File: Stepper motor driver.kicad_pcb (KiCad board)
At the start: 2 copper layers, 63 x 74.4 mm, 24 parts, among them Q1 TIP120, Q2 TIP120, Q3 TIP120, Q4 TIP120, U1 74LS175, U2 74LS157

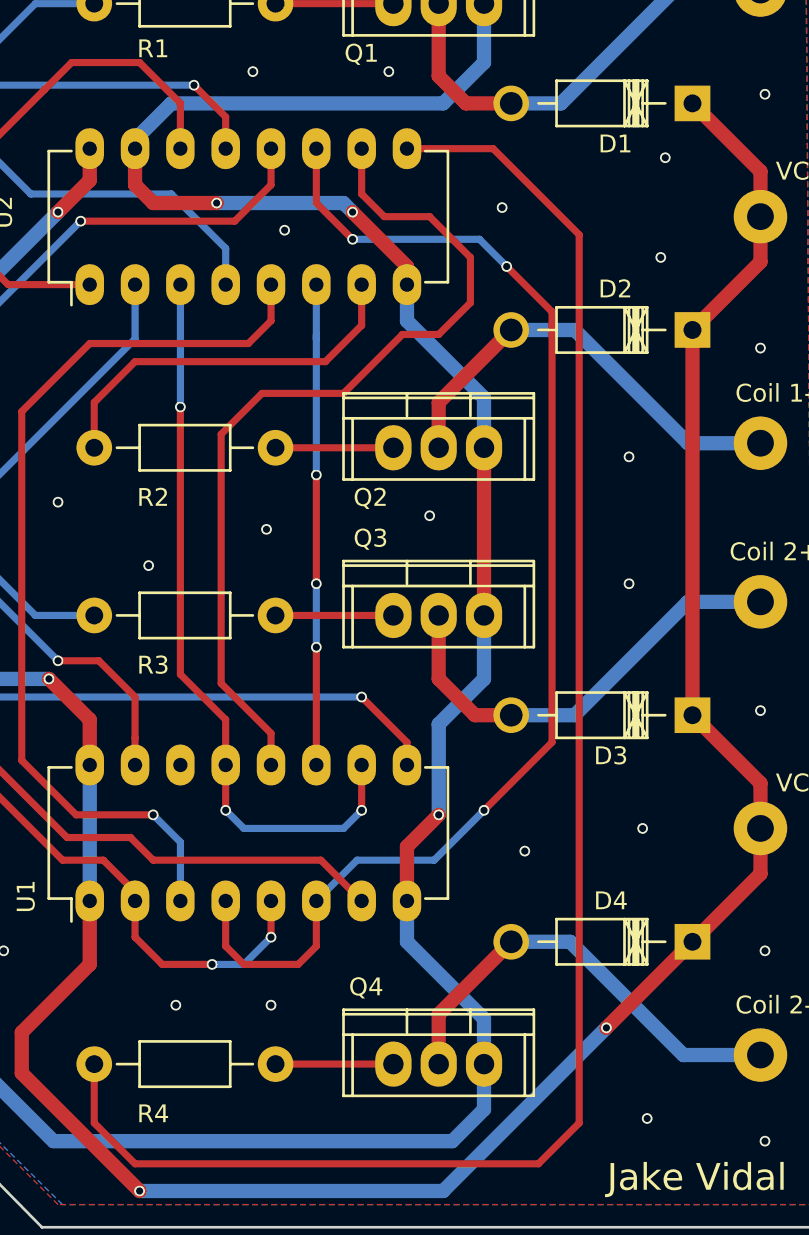
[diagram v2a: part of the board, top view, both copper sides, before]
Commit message: added additional vias
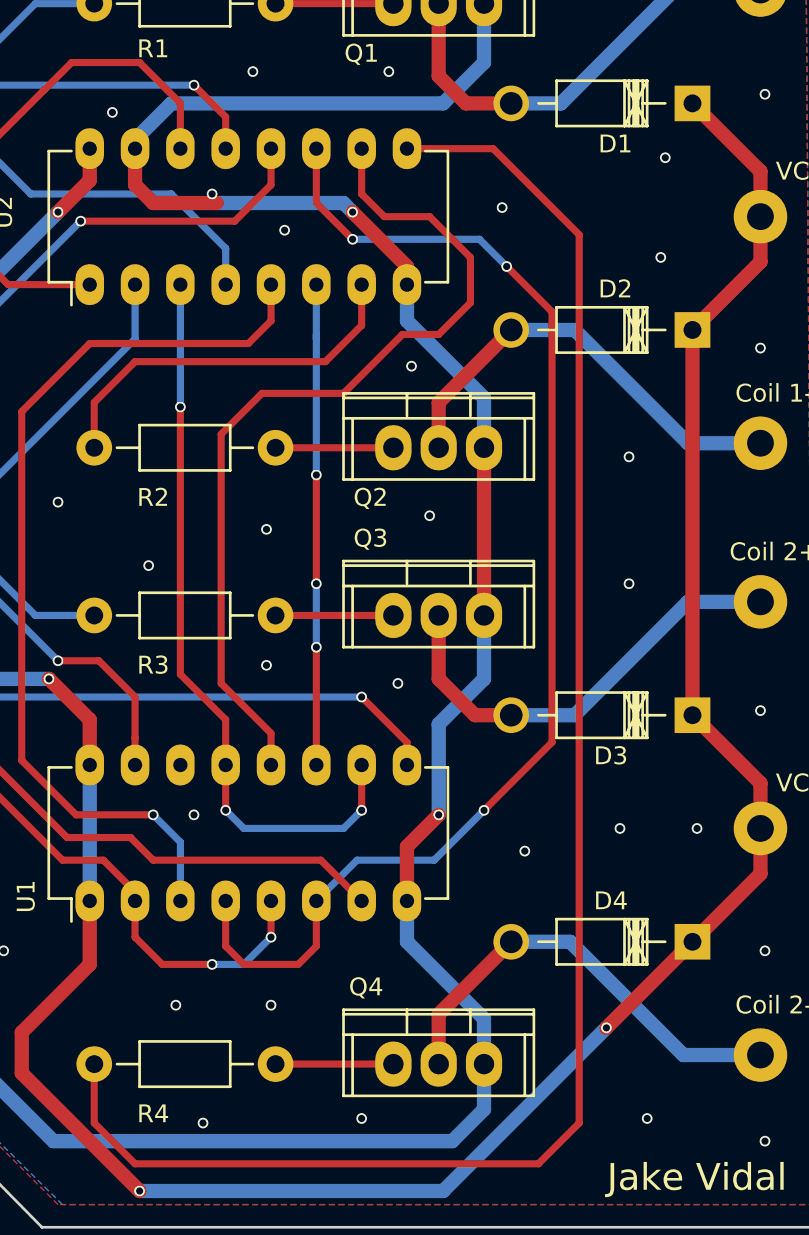
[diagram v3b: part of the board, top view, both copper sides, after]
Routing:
- net GND: vias 39 -> 4
- net (no net): vias 0 -> 43
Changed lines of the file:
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@@
     (thickness 1.6)
     (drawings 7)
-    (tracks 290)
+    (tracks 298)
     (zones 0)
     (modules 24)
@@
   (gr_line (start 215 20.32) (end 196.596 38) (angle 90) (layer Edge.Cuts) (width 0.15))
   (gr_line (start 259.588 20.32) (end 215 20.32) (angle 90) (layer Edge.Cuts) (width 0.15))
+  (via (at 235.712 46.482) (size 0.6) (drill 0.4) (layers F.Cu B.Cu) (net 0))
+  (via (at 251.714 72.39) (size 0.6) (drill 0.4) (layers F.Cu B.Cu) (net 0))
+  (via (at 228.6 38.862) (size 0.6) (drill 0.4) (layers F.Cu B.Cu) (net 0))
+  (via (at 240.792 37.592) (size 0.6) (drill 0.4) (layers F.Cu B.Cu) (net 0))
+  (via (at 255.524 89.916) (size 0.6) (drill 0.4) (layers F.Cu B.Cu) (net 0))
+  (via (at 207.01 72.39) (size 0.6) (drill 0.4) (layers F.Cu B.Cu) (net 0))
+  (via (at 212.09 73.66) (size 0.6) (drill 0.4) (layers F.Cu B.Cu) (net 0))
+  (via (at 207.772 63.246) (size 0.6) (drill 0.4) (layers F.Cu B.Cu) (net 0))
+  (via (at 200.914 68.326) (size 0.6) (drill 0.4) (layers F.Cu B.Cu) (net 0))
+  (via (at 200.406 56.896) (size 0.6) (drill 0.4) (layers F.Cu B.Cu) (net 0))
+  (via (at 206.248 54.356) (size 0.6) (drill 0.4) (layers F.Cu B.Cu) (net 0))
+  (via (at 206.756 41.402) (size 0.6) (drill 0.4) (layers F.Cu B.Cu) (net 0))
+  (via (at 199.39 44.958) (size 0.6) (drill 0.4) (layers F.Cu B.Cu) (net 0))
+  (via (at 205.486 35.052) (size 0.6) (drill 0.4) (layers F.Cu B.Cu) (net 0))
+  (via (at 216.408 23.622) (size 0.6) (drill 0.4) (layers F.Cu B.Cu) (net 0))
+  (via (at 226.314 23.368) (size 0.6) (drill 0.4) (layers F.Cu B.Cu) (net 0))
+  (via (at 226.822 29.972) (size 0.6) (drill 0.4) (layers F.Cu B.Cu) (net 0))
+  (via (at 234.442 29.972) (size 0.6) (drill 0.4) (layers F.Cu B.Cu) (net 0))
+  (via (at 245.872 24.384) (size 0.6) (drill 0.4) (layers F.Cu B.Cu) (net 0))
+  (via (at 255.524 31.242) (size 0.6) (drill 0.4) (layers F.Cu B.Cu) (net 0))
+  (via (at 249.936 34.798) (size 0.6) (drill 0.4) (layers F.Cu B.Cu) (net 0))
+  (via (at 249.682 40.386) (size 0.6) (drill 0.4) (layers F.Cu B.Cu) (net 0))
+  (via (at 255.27 45.466) (size 0.6) (drill 0.4) (layers F.Cu B.Cu) (net 0))
+  (via (at 215.9 54.102) (size 0.6) (drill 0.4) (layers F.Cu B.Cu) (net 0))
+  (via (at 220.98 57.658) (size 0.6) (drill 0.4) (layers F.Cu B.Cu) (net 0))
+  (via (at 227.584 55.626) (size 0.6) (drill 0.4) (layers F.Cu B.Cu) (net 0))
+  (via (at 236.728 54.864) (size 0.6) (drill 0.4) (layers F.Cu B.Cu) (net 0))
+  (via (at 247.904 51.562) (size 0.6) (drill 0.4) (layers F.Cu B.Cu) (net 0))
+  (via (at 247.904 58.674) (size 0.6) (drill 0.4) (layers F.Cu B.Cu) (net 0))
+  (via (at 255.27 65.786) (size 0.6) (drill 0.4) (layers F.Cu B.Cu) (net 0))
+  (via (at 242.062 73.66) (size 0.6) (drill 0.4) (layers F.Cu B.Cu) (net 0))
+  (via (at 255.524 79.248) (size 0.6) (drill 0.4) (layers F.Cu B.Cu) (net 0))
+  (via (at 248.92 88.646) (size 0.6) (drill 0.4) (layers F.Cu B.Cu) (net 0))
+  (via (at 227.838 82.296) (size 0.6) (drill 0.4) (layers F.Cu B.Cu) (net 0))
+  (via (at 222.504 82.296) (size 0.6) (drill 0.4) (layers F.Cu B.Cu) (net 0))
+  (via (at 212.852 79.248) (size 0.6) (drill 0.4) (layers F.Cu B.Cu) (net 0))
+  (via (at 205.74 79.756) (size 0.6) (drill 0.4) (layers F.Cu B.Cu) (net 0))
+  (via (at 247.396 72.39) (size 0.6) (drill 0.4) (layers F.Cu B.Cu) (net 0))
+  (via (at 234.95 64.262) (size 0.6) (drill 0.4) (layers F.Cu B.Cu) (net 0))
+  (via (at 223.52 71.628) (size 0.6) (drill 0.4) (layers F.Cu B.Cu) (net 0))
+  (via (at 232.918 88.646) (size 0.6) (drill 0.4) (layers F.Cu B.Cu) (net 0))
+  (via (at 224.028 88.9) (size 0.6) (drill 0.4) (layers F.Cu B.Cu) (net 0))
+  (via (at 224.536 36.83) (size 0.6) (drill 0.4) (layers F.Cu B.Cu) (net 0))
   (segment (start 241.3 31.75254) (end 244.09146 31.75254) (width 0.8) (layer B.Cu) (net 1))
   (segment (start 250.444 25.4) (end 255.27 25.4) (width 0.8) (layer B.Cu) (net 1))
@@
   (segment (start 237.236 85.598) (end 237.236 82.80654) (width 0.8) (layer F.Cu) (net 4))
   (segment (start 237.236 82.80654) (end 241.3 78.74254) (width 0.8) (layer F.Cu) (net 4))
-  (via (at 228.6 38.862) (size 0.6) (drill 0.4) (layers F.Cu B.Cu) (net 5))
-  (via (at 240.792 37.592) (size 0.6) (drill 0.4) (layers F.Cu B.Cu) (net 5))
-  (via (at 255.524 89.916) (size 0.6) (drill 0.4) (layers F.Cu B.Cu) (net 5))
-  (via (at 207.01 72.39) (size 0.6) (drill 0.4) (layers F.Cu B.Cu) (net 5))
-  (via (at 212.09 73.66) (size 0.6) (drill 0.4) (layers F.Cu B.Cu) (net 5))
-  (via (at 207.772 63.246) (size 0.6) (drill 0.4) (layers F.Cu B.Cu) (net 5))
-  (via (at 200.914 68.326) (size 0.6) (drill 0.4) (layers F.Cu B.Cu) (net 5))
-  (via (at 200.406 56.896) (size 0.6) (drill 0.4) (layers F.Cu B.Cu) (net 5))
-  (via (at 206.248 54.356) (size 0.6) (drill 0.4) (layers F.Cu B.Cu) (net 5))
-  (via (at 206.756 41.402) (size 0.6) (drill 0.4) (layers F.Cu B.Cu) (net 5))
-  (via (at 199.39 44.958) (size 0.6) (drill 0.4) (layers F.Cu B.Cu) (net 5))
-  (via (at 205.486 35.052) (size 0.6) (drill 0.4) (layers F.Cu B.Cu) (net 5))
-  (via (at 216.408 23.622) (size 0.6) (drill 0.4) (layers F.Cu B.Cu) (net 5))
-  (via (at 226.314 23.368) (size 0.6) (drill 0.4) (layers F.Cu B.Cu) (net 5))
-  (via (at 226.822 29.972) (size 0.6) (drill 0.4) (layers F.Cu B.Cu) (net 5))
-  (via (at 234.442 29.972) (size 0.6) (drill 0.4) (layers F.Cu B.Cu) (net 5))
-  (via (at 245.872 24.384) (size 0.6) (drill 0.4) (layers F.Cu B.Cu) (net 5))
-  (via (at 255.524 31.242) (size 0.6) (drill 0.4) (layers F.Cu B.Cu) (net 5))
-  (via (at 249.936 34.798) (size 0.6) (drill 0.4) (layers F.Cu B.Cu) (net 5))
-  (via (at 249.682 40.386) (size 0.6) (drill 0.4) (layers F.Cu B.Cu) (net 5))
-  (via (at 255.27 45.466) (size 0.6) (drill 0.4) (layers F.Cu B.Cu) (net 5))
-  (via (at 215.9 54.102) (size 0.6) (drill 0.4) (layers F.Cu B.Cu) (net 5))
-  (via (at 220.98 57.658) (size 0.6) (drill 0.4) (layers F.Cu B.Cu) (net 5))
-  (via (at 227.584 55.626) (size 0.6) (drill 0.4) (layers F.Cu B.Cu) (net 5))
-  (via (at 236.728 54.864) (size 0.6) (drill 0.4) (layers F.Cu B.Cu) (net 5))
-  (via (at 247.904 51.562) (size 0.6) (drill 0.4) (layers F.Cu B.Cu) (net 5))
-  (via (at 247.904 58.674) (size 0.6) (drill 0.4) (layers F.Cu B.Cu) (net 5))
-  (via (at 255.27 65.786) (size 0.6) (drill 0.4) (layers F.Cu B.Cu) (net 5))
-  (via (at 242.062 73.66) (size 0.6) (drill 0.4) (layers F.Cu B.Cu) (net 5))
-  (via (at 248.666 72.39) (size 0.6) (drill 0.4) (layers F.Cu B.Cu) (net 5))
-  (via (at 255.524 79.248) (size 0.6) (drill 0.4) (layers F.Cu B.Cu) (net 5))
-  (via (at 248.92 88.646) (size 0.6) (drill 0.4) (layers F.Cu B.Cu) (net 5))
-  (via (at 227.838 82.296) (size 0.6) (drill 0.4) (layers F.Cu B.Cu) (net 5))
-  (via (at 222.504 82.296) (size 0.6) (drill 0.4) (layers F.Cu B.Cu) (net 5))
-  (via (at 212.852 79.248) (size 0.6) (drill 0.4) (layers F.Cu B.Cu) (net 5))
-  (via (at 205.74 79.756) (size 0.6) (drill 0.4) (layers F.Cu B.Cu) (net 5))
+  (via (at 227.584 63.246) (size 0.6) (drill 0.4) (layers F.Cu B.Cu) (net 5))
+  (via (at 218.948 32.258) (size 0.6) (drill 0.4) (layers F.Cu B.Cu) (net 5))
   (segment (start 220.218 34.29) (end 220.218 33.782) (width 0.8) (layer B.Cu) (net 5))
   (segment (start 220.218 33.782) (end 222.25 31.75) (width 0.8) (layer B.Cu) (net 5))
@@
   (segment (start 221.234 37.338) (end 220.218 36.322) (width 0.8) (layer F.Cu) (net 5))
   (segment (start 224.79 37.338) (end 221.234 37.338) (width 0.8) (layer F.Cu) (net 5))
-  (via (at 224.79 37.338) (size 0.6) (drill 0.4) (layers F.Cu B.Cu) (net 5))
   (segment (start 231.902 37.338) (end 224.79 37.338) (width 0.8) (layer B.Cu) (net 5))
   (segment (start 232.41 37.846) (end 231.902 37.338) (width 0.8) (layer B.Cu) (net 5))

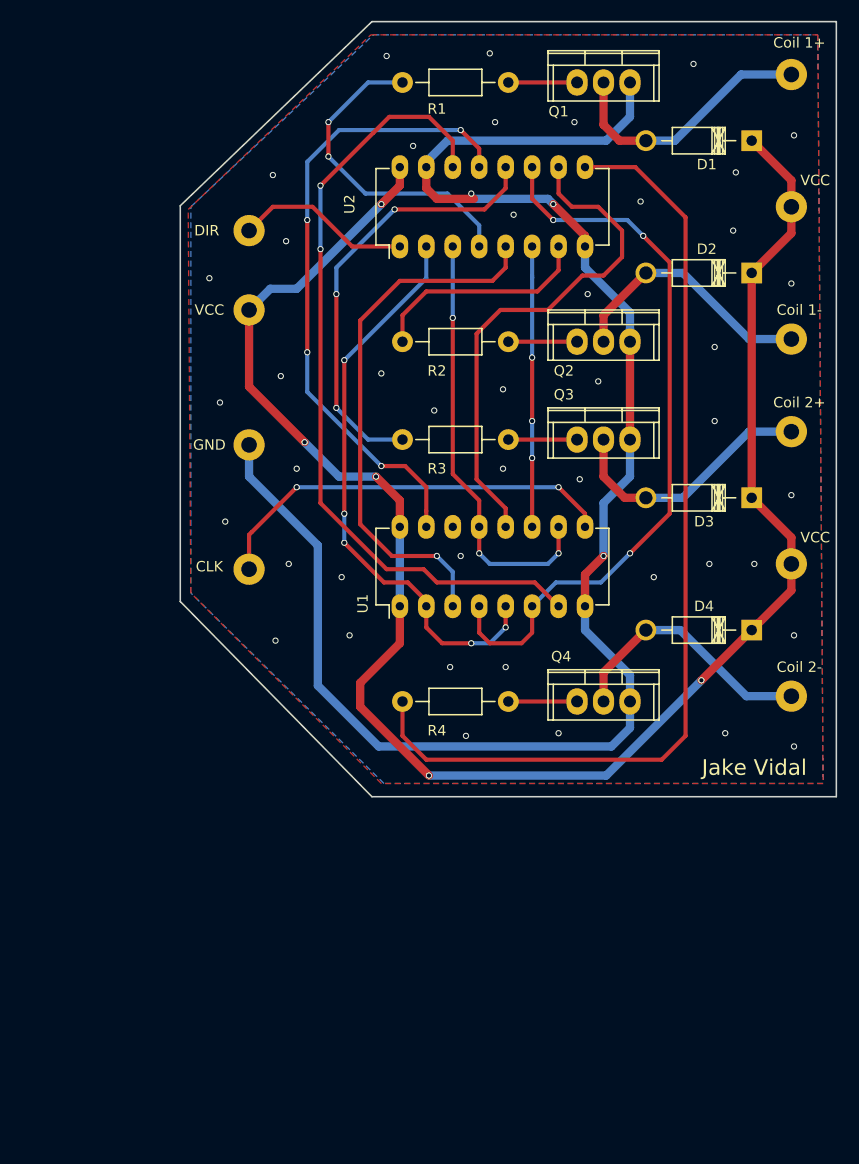
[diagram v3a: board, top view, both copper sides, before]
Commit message: Added connectors for I/O and changed to SMD components
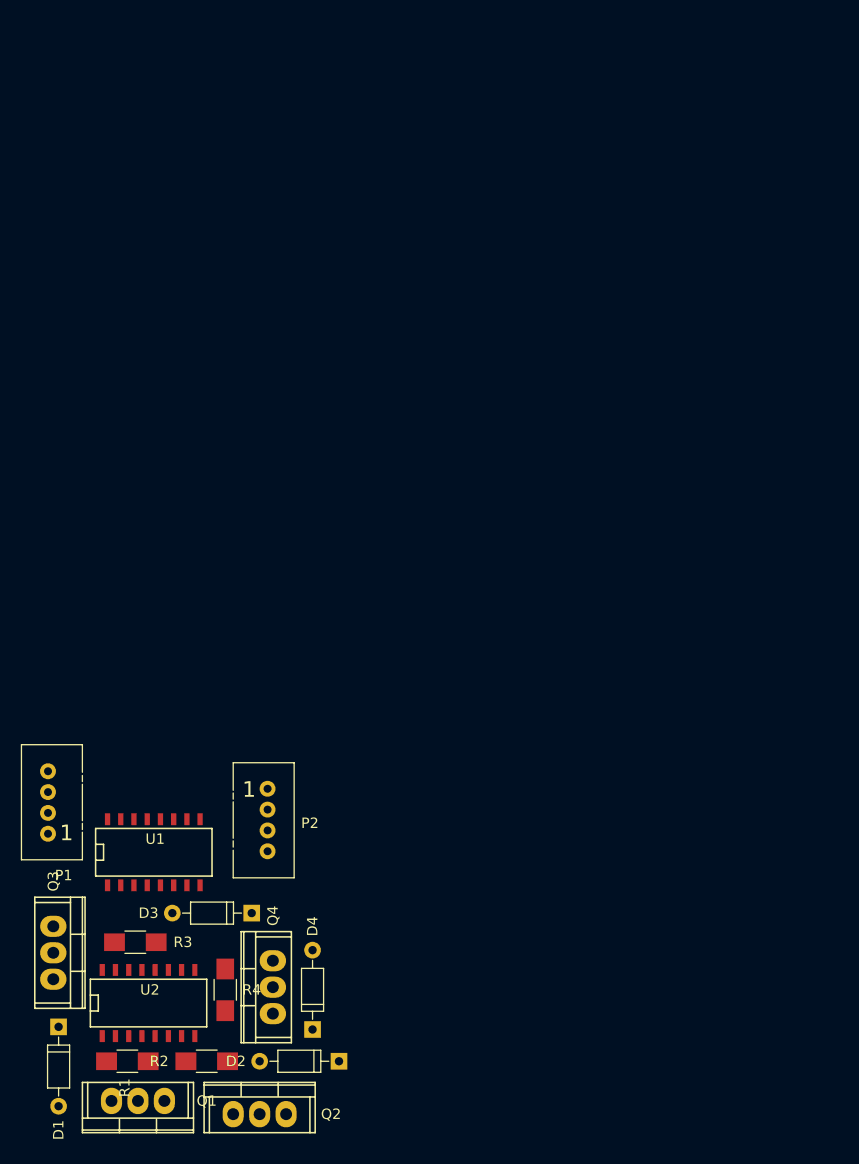
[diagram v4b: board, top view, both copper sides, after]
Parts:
- removed CLK, DIR, GND, VCC (x3): TEST_1P, Measurement_Points:Measurement_Point_Round-TH_Big
- removed Coil 1+: TEST_1P, Measurement_Points:Measurement_Point_Round-TH_Big
- removed Coil 1-: TEST_1P, Measurement_Points:Measurement_Point_Round-TH_Big
- removed Coil 2+: TEST_1P, Measurement_Points:Measurement_Point_Round-TH_Big
- removed Coil 2-: TEST_1P, Measurement_Points:Measurement_Point_Round-TH_Big
- added P1: CONN_01X04, Connect:Grove_1x04, F.Cu at (183.9, 98.3)
- added P2: CONN_01X04, Connect:Grove_1x04, F.Cu at (205.0, 94.0)
- D1, D2, D3, D4: footprint Diodes_ThroughHole:Diode_DO-41_SOD81_Horizontal_RM10 -> Diodes_ThroughHole:D_DO-35_SOD27_P7.62mm_Horizontal
- R1, R2, R3, R4: footprint Resistors_ThroughHole:Resistor_Horizontal_RM10mm -> Resistors_SMD:R_1206_HandSoldering
- U1, U2: footprint Housings_DIP:DIP-16_W7.62mm_LongPads -> SMD_Packages:SO-16-N
- moved D1 108.0 mm to (184.9, 116.8), turned to 270 degrees
- moved Q1 107.5 mm to (192.5, 124.0), turned to 180 degrees
- moved R1 100.8 mm to (191.5, 120.1), turned to 0 degrees
- moved D2 85.4 mm to (211.8, 120.1)
- moved Q2 81.2 mm to (204.2, 125.2)
- moved U2 76.5 mm to (193.5, 114.6), turned to 0 degrees
- moved R2 74.9 mm to (199.1, 120.1)
- moved Q3 72.2 mm to (184.4, 109.7), turned to 270 degrees
- moved D3 62.4 mm to (203.5, 105.9)
- moved R3 60.1 mm to (192.3, 108.7), turned to 0 degrees
- moved D4 57.0 mm to (209.3, 117.1), turned to 90 degrees
- moved Q4 42.0 mm to (205.5, 113.0), turned to 90 degrees
- moved R4 38.8 mm to (200.9, 113.3), turned to 90 degrees
- moved U1 33.4 mm to (194.1, 100.1), turned to 0 degrees
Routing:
- net VCC: track 168.4 -> 0.00 mm, vias 5 -> 0
- net GND: track 155.9 -> 0.00 mm, vias 4 -> 0
- net Net-(R4-Pad2): track 93.8 -> 0.00 mm
- net /A1-: track 76.4 -> 0.00 mm, vias 2 -> 0
- net /A1+: track 70.8 -> 0.00 mm, vias 3 -> 0
- net /B2+: track 61.4 -> 0.00 mm, vias 4 -> 0
- net /B1+: track 55.4 -> 0.00 mm, vias 5 -> 0
- net /B1-: track 51.7 -> 0.00 mm, vias 1 -> 0
- net /B2-: track 49.4 -> 0.00 mm
- net Net-(R3-Pad2): track 42.5 -> 0.00 mm, vias 3 -> 0
- net /A2-: track 41.5 -> 0.00 mm, vias 3 -> 0
- net /CLK: track 39.8 -> 0.00 mm, vias 2 -> 0
- net Net-(R1-Pad2): track 31.2 -> 0.00 mm, vias 2 -> 0
- net /A2+: track 27.2 -> 0.00 mm, vias 3 -> 0
- net Net-(D1-Pad2): track 25.4 -> 0.00 mm
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- removed copper zone on B.Cu, net GND
- removed copper zone on F.Cu, net GND
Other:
- board outline removed
- board text removed: "Jake Vidal"
